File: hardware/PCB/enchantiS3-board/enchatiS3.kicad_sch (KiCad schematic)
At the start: 71 parts, among them J1 USB_C_Receptacle_USB2.0, Q1 BSS138, Q2 BSS138, Q3 BSS138, SW1 B3U-1000P, SW2 B3U-1000P, U1 USBLC6-2P6, U2 MCP73871, U3 NCP167AMX330TBG, U4 NCP167AMX180TBG

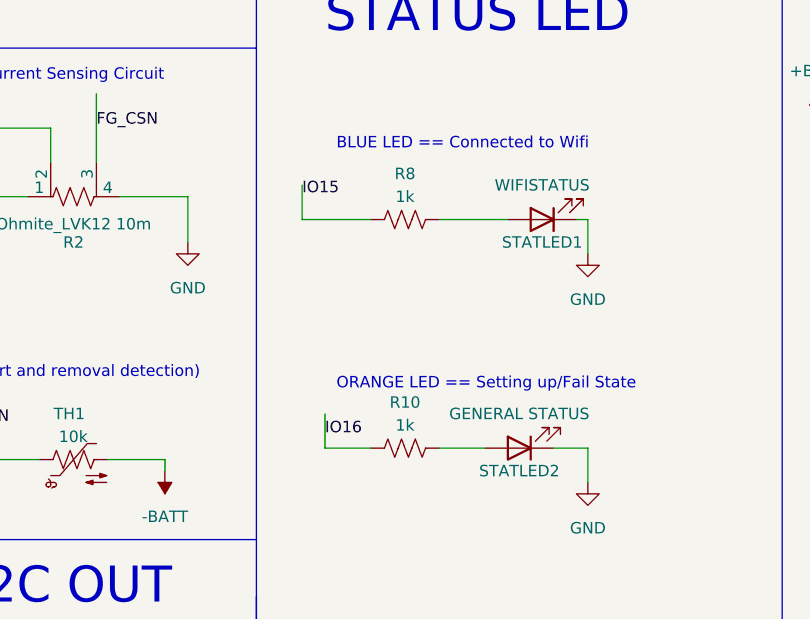
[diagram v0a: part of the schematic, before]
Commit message: rename PCB files to enchantiS3, exposed SPI pins for touch board
Renamed ESP32 board PCB files to EnchantiS3
Exposed SPI pins for enchanti touch board
Changed Aux touch board connector to two 4 pin JST SM connectors
Updated Enchanti touch board BOM an manufacturing files
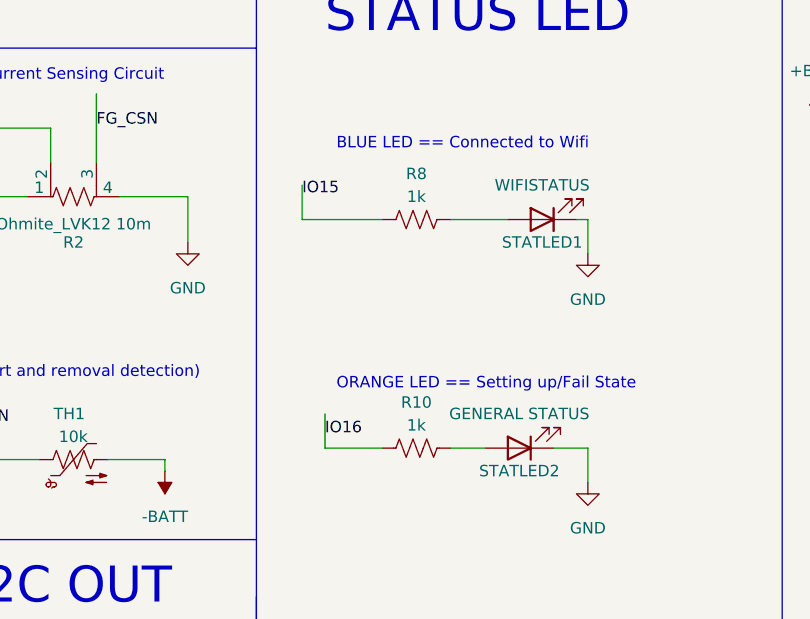
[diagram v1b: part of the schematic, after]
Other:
- moved on the sheet: R10, R8
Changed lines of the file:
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@@
     (stroke (width 0) (type default))
   )
-  (wire (pts (xy 294.64 165.1) (xy 299.72 165.1))
+  (wire (pts (xy 295.91 165.1) (xy 299.72 165.1))
     (stroke (width 0) (type default))
   )
@@
     (stroke (width 0) (type default))
   )
-  (wire (pts (xy 279.4 139.7) (xy 287.02 139.7))
+  (wire (pts (xy 279.4 139.7) (xy 288.29 139.7))
     (stroke (width 0) (type default))
   )
@@
     (stroke (width 0) (type default))
   )
-  (wire (pts (xy 294.64 139.7) (xy 302.26 139.7))
+  (wire (pts (xy 295.91 139.7) (xy 302.26 139.7))
     (stroke (width 0) (type default))
   )
@@
     (stroke (width 0) (type default))
   )
-  (wire (pts (xy 281.94 165.1) (xy 287.02 165.1))
+  (wire (pts (xy 281.94 165.1) (xy 288.29 165.1))
     (stroke (width 0) (type default))
   )
@@
     (effects (font (size 1.27 1.27)) (justify left bottom))
   )
-  (symbol (lib_id "Device:R_US") (at 290.83 139.7 90) (unit 1)
+  (symbol (lib_id "Device:R_US") (at 292.1 139.7 90) (unit 1)
     (in_bom yes) (on_board yes) (dnp no)
-    (property "Reference" "R8" (at 290.83 134.62 90)
-      (effects (font (size 1.27 1.27)))
-    )
-    (property "Value" "1k" (at 290.83 137.16 90)
-      (effects (font (size 1.27 1.27)))
-    )
-    (property "Footprint" "Resistor_SMD:R_0402_1005Metric" (at 291.084 138.684 90)
-      (effects (font (size 1.27 1.27)) hide)
-    )
-    (property "Datasheet" "https://industrial.panasonic.com/cdbs/www-data/pdf/RDA0000/AOA0000C304.pdf" (at 290.83 139.7 0)
-      (effects (font (size 1.27 1.27)) hide)
-    )
-    (property "Description Value Pkg" "1 kOhms ±1% 0.1W, 1/10W Chip Resistor 0402 (1005 Metric) Automotive AEC-Q200 Thick Film" (at 290.83 139.7 0)
-      (effects (font (size 1.27 1.27)) hide)
-    )
-    (property "Mfg Part #" "ERJ-2RKF1001X" (at 290.83 139.7 0)
-      (effects (font (size 1.27 1.27)) hide)
-    )
-    (property "Manufacturer" "Panasonic Electronic Components" (at 290.83 139.7 0)
-      (effects (font (size 1.27 1.27)) hide)
-    )
-    (property "mpn" "ERJ-2RKF1001X" (at 290.83 139.7 0)
+    (property "Reference" "R8" (at 292.1 134.62 90)
+      (effects (font (size 1.27 1.27)))
+    )
+    (property "Value" "1k" (at 292.1 137.16 90)
+      (effects (font (size 1.27 1.27)))
+    )
+    (property "Footprint" "Resistor_SMD:R_0402_1005Metric" (at 292.354 138.684 90)
+      (effects (font (size 1.27 1.27)) hide)
+    )
+    (property "Datasheet" "https://industrial.panasonic.com/cdbs/www-data/pdf/RDA0000/AOA0000C304.pdf" (at 292.1 139.7 0)
+      (effects (font (size 1.27 1.27)) hide)
+    )
+    (property "Description Value Pkg" "1 kOhms ±1% 0.1W, 1/10W Chip Resistor 0402 (1005 Metric) Automotive AEC-Q200 Thick Film" (at 292.1 139.7 0)
+      (effects (font (size 1.27 1.27)) hide)
+    )
+    (property "Mfg Part #" "ERJ-2RKF1001X" (at 292.1 139.7 0)
+      (effects (font (size 1.27 1.27)) hide)
+    )
+    (property "Manufacturer" "Panasonic Electronic Components" (at 292.1 139.7 0)
+      (effects (font (size 1.27 1.27)) hide)
+    )
+    (property "mpn" "ERJ-2RKF1001X" (at 292.1 139.7 0)
       (effects (font (size 1.27 1.27)) hide)
     )
@@
     )
   )
-  (symbol (lib_id "Device:R_US") (at 290.83 165.1 90) (unit 1)
+  (symbol (lib_id "Device:R_US") (at 292.1 165.1 90) (unit 1)
     (in_bom yes) (on_board yes) (dnp no)
-    (property "Reference" "R10" (at 290.83 160.02 90)
-      (effects (font (size 1.27 1.27)))
-    )
-    (property "Value" "1k" (at 290.83 162.56 90)
-      (effects (font (size 1.27 1.27)))
-    )
-    (property "Footprint" "Resistor_SMD:R_0402_1005Metric" (at 291.084 164.084 90)
-      (effects (font (size 1.27 1.27)) hide)
-    )
-    (property "Datasheet" "https://industrial.panasonic.com/cdbs/www-data/pdf/RDA0000/AOA0000C304.pdf" (at 290.83 165.1 0)
-      (effects (font (size 1.27 1.27)) hide)
-    )
-    (property "Description Value Pkg" "1 kOhms ±1% 0.1W, 1/10W Chip Resistor 0402 (1005 Metric) Automotive AEC-Q200 Thick Film" (at 290.83 165.1 0)
-      (effects (font (size 1.27 1.27)) hide)
-    )
-    (property "Mfg Part #" "ERJ-2RKF1001X" (at 290.83 165.1 0)
-      (effects (font (size 1.27 1.27)) hide)
-    )
-    (property "Manufacturer" "Panasonic Electronic Components" (at 290.83 165.1 0)
-      (effects (font (size 1.27 1.27)) hide)
-    )
-    (property "mpn" "ERJ-2RKF1001X" (at 290.83 165.1 0)
-      (effects (font (size 1.27 1.27)) hide)
-    )
+    (property "Reference" "R10" (at 292.1 160.02 90)
+      (effects (font (size 1.27 1.27)))
+    )
+    (property "Value" "1k" (at 292.1 162.56 90)
+      (effects (font (size 1.27 1.27)))
+    )
+    (property "Footprint" "Resistor_SMD:R_0402_1005Metric" (at 292.354 164.084 90)
+      (effects (font (size 1.27 1.27)) hide)
+    )
+    (property "Datasheet" "https://industrial.panasonic.com/cdbs/www-data/pdf/RDA0000/AOA0000C304.pdf" (at 292.1 165.1 0)
+      (effects (font (size 1.27 1.27)) hide)
+    )
+    (property "Description Value Pkg" "1 kOhms ±1% 0.1W, 1/10W Chip Resistor 0402 (1005 Metric) Automotive AEC-Q200 Thick Film" (at 292.1 165.1 0)
+      (effects (font (size 1.27 1.27)) hide)
+    )
+    (property "Mfg Part #" "ERJ-2RKF1001X" (at 292.1 165.1 0)
+      (effects (font (size 1.27 1.27)) hide)
+    )
+    (property "Manufacturer" "Panasonic Electronic Components" (at 292.1 165.1 0)
+      (effects (font (size 1.27 1.27)) hide)
+    )
+    (property "mpn" "ERJ-2RKF1001X" (at 292.1 165.1 0)
+      (effects (font (size 1.27 1.27)) hide)
+    )
